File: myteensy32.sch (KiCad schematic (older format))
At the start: 31 parts, among them J1 Conn_01x14_Male, J2 Conn_01x14_Male, J3 USB_C_Receptacle_USB2.0, SW1 RESET, SW2 PROG, U1 MKL04Z32VLC4, U2 MK20DX256VLH7, U3 MCP2562-E-SN, U4 LT1117-3.3, Y2 16MHz

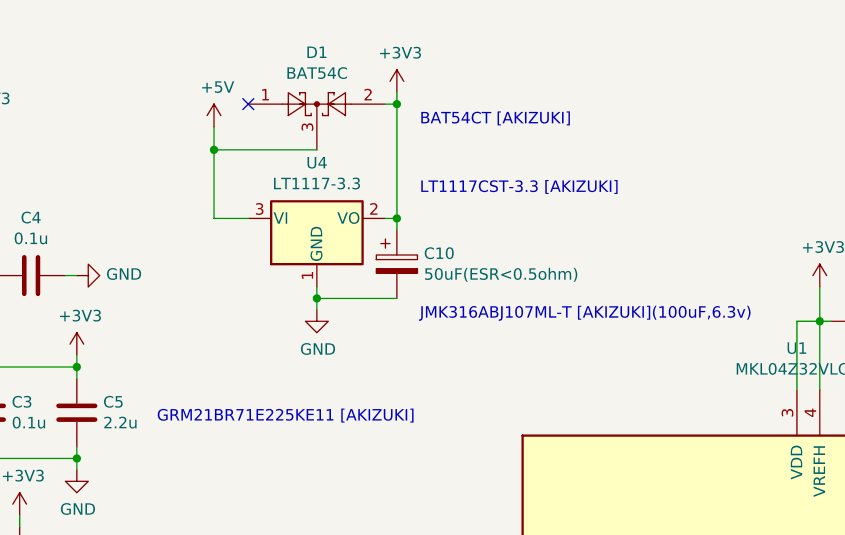
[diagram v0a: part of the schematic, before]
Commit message: 回路図中のレギュレータを変更
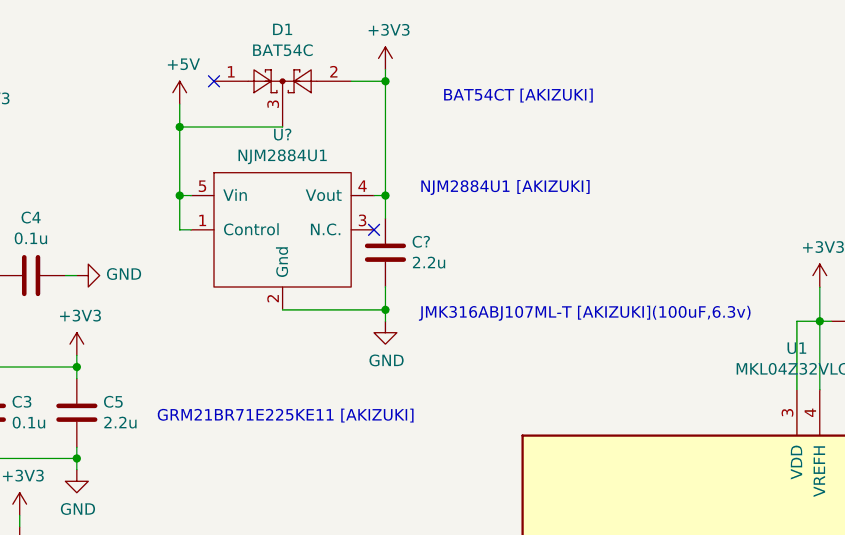
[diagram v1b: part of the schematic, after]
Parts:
- removed C10: 50uF(ESR<0.5ohm), Capacitor_SMD:C_1206_3216Metric, symbol Device:CP
- removed U4: LT1117-3.3, Package_TO_SOT_SMD:SOT-223-3_TabPin2, symbol Regulator_Linear:LT1117-3.3
- added C?: 2.2u, Capacitor_SMD:C_0805_2012Metric, symbol Device:C
- added U?: NJM2884U1, Package_TO_SOT_SMD:SOT-89-5, symbol mylib:NJM2884U1
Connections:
- net +3V3: now also C?.1, U?.4 (Vout)
- net +5V: now also U?.1 (Control), U?.5 (Vin)
- net GND: now also C?.2, U?.2 (Gnd)
- no-connect marks 30 -> 31
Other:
- note added: "NJM2884U1 [AKIZUKI]"
- note removed: "LT1117CST-3.3 [AKIZUKI]"
- moved on the sheet: D1
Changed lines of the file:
@@
 ProgramModeBtn
-$Comp
-L Regulator_Linear:LT1117-3.3 U4
-U 1 1 5F744D1C
-P 6100 1450
-F 0 "U4" H 6100 1692 50  0000 C CNN
-F 1 "LT1117-3.3" H 6100 1601 50  0000 C CNN
-F 2 "Package_TO_SOT_SMD:SOT-223-3_TabPin2" H 6100 1450 50  0001 C CNN
-F 3 "https://www.analog.com/media/en/technical-documentation/data-sheets/1117fd.pdf" H 6100 1450 50  0001 C CNN
-	1    6100 1450
-	1    0    0    -1
-$EndComp
-$Comp
-L Device:CP C10
-U 1 1 5F749F5F
-P 6450 1650
-F 0 "C10" H 6568 1696 50  0000 L CNN
-F 1 "50uF(ESR<0.5ohm)" H 6568 1605 50  0000 L CNN
-F 2 "Capacitor_SMD:C_1206_3216Metric" H 6488 1500 50  0001 C CNN
-F 3 "~" H 6450 1650 50  0001 C CNN
-	1    6450 1650
-	1    0    0    -1
-$EndComp
-Wire Wire Line
-	6450 1450 6400 1450
-Wire Wire Line
-	5800 1450 5650 1450
-Wire Wire Line
-	6450 1500 6450 1450
-Connection ~ 6450 1450
-Wire Wire Line
-	6450 1800 6100 1800
-Wire Wire Line
-	6100 1800 6100 1750
 $Comp
 L power:+3V3 #PWR0118
 U 1 1 5F7BEC67
-P 6450 900
-F 0 "#PWR0118" H 6450 750 50  0001 C CNN
-F 1 "+3V3" H 6465 1073 50  0000 C CNN
-F 2 "" H 6450 900 50  0001 C CNN
-F 3 "" H 6450 900 50  0001 C CNN
-	1    6450 900
+P 6400 800
+F 0 "#PWR0118" H 6400 650 50  0001 C CNN
+F 1 "+3V3" H 6415 973 50  0000 C CNN
+F 2 "" H 6400 800 50  0001 C CNN
+F 3 "" H 6400 800 50  0001 C CNN
+	1    6400 800
 	1    0    0    -1
 $EndComp
@@
 L power:GND #PWR0119
 U 1 1 5F7C2F97
-P 6100 1850
-F 0 "#PWR0119" H 6100 1600 50  0001 C CNN
-F 1 "GND" H 6105 1677 50  0000 C CNN
-F 2 "" H 6100 1850 50  0001 C CNN
-F 3 "" H 6100 1850 50  0001 C CNN
-	1    6100 1850
-	1    0    0    -1
-$EndComp
-Wire Wire Line
-	6100 1850 6100 1800
-Connection ~ 6100 1800
+P 6400 1900
+F 0 "#PWR0119" H 6400 1650 50  0001 C CNN
+F 1 "GND" H 6405 1727 50  0000 C CNN
+F 2 "" H 6400 1900 50  0001 C CNN
+F 3 "" H 6400 1900 50  0001 C CNN
+	1    6400 1900
+	1    0    0    -1
+$EndComp
+Wire Wire Line
+	6400 1900 6400 1850
 $Comp
 L power:+5V #PWR0120
 U 1 1 5F7C741A
-P 5650 1050
-F 0 "#PWR0120" H 5650 900 50  0001 C CNN
-F 1 "+5V" H 5665 1223 50  0000 C CNN
-F 2 "" H 5650 1050 50  0001 C CNN
-F 3 "" H 5650 1050 50  0001 C CNN
-	1    5650 1050
+P 5500 950
+F 0 "#PWR0120" H 5500 800 50  0001 C CNN
+F 1 "+5V" H 5515 1123 50  0000 C CNN
+F 2 "" H 5500 950 50  0001 C CNN
+F 3 "" H 5500 950 50  0001 C CNN
+	1    5500 950
 	1    0    0    -1
 $EndComp
@@
 MF-FSMF035X-2 [AKIZUKI]
 Text Notes 6550 1350 0    50   ~ 0
-LT1117CST-3.3 [AKIZUKI]
-Text Notes 6550 1050 0    50   ~ 0
+NJM2884U1 [AKIZUKI]
+Text Notes 6650 950  0    50   ~ 0
 BAT54CT [AKIZUKI]
 $Comp
@@
 L Diode:BAT54C D1
 U 1 1 5FA3A467
-P 6100 950
-F 0 "D1" H 6100 1175 50  0000 C CNN
-F 1 "BAT54C" H 6100 1084 50  0000 C CNN
-F 2 "Package_TO_SOT_SMD:SOT-23" H 6175 1075 50  0001 L CNN
-F 3 "http://www.diodes.com/_files/datasheets/ds11005.pdf" H 6020 950 50  0001 C CNN
-	1    6100 950
-	1    0    0    -1
-$EndComp
-Wire Wire Line
-	6450 900  6450 950
-Wire Wire Line
-	5650 1050 5650 1150
-Wire Wire Line
-	6450 950  6400 950
-Connection ~ 6450 950
-Wire Wire Line
-	6450 950  6450 1450
-Wire Wire Line
-	6100 1150 5650 1150
-Connection ~ 5650 1150
-Wire Wire Line
-	5650 1150 5650 1450
-NoConn ~ 5800 950
+P 5950 850
+F 0 "D1" H 5950 1075 50  0000 C CNN
+F 1 "BAT54C" H 5950 984 50  0000 C CNN
+F 2 "Package_TO_SOT_SMD:SOT-23" H 6025 975 50  0001 L CNN
+F 3 "http://www.diodes.com/_files/datasheets/ds11005.pdf" H 5870 850 50  0001 C CNN
+	1    5950 850
+	1    0    0    -1
+$EndComp
+Wire Wire Line
+	6400 800  6400 850
+Wire Wire Line
+	6400 850  6250 850
+Connection ~ 6400 850
+Wire Wire Line
+	6400 850  6400 1350
+NoConn ~ 5650 850
 Text Notes 10200 4400 0    50   ~ 0
 SW1020CT-ND [digikey](b3u-1000p)
@@
 NoConn ~ 4600 4000
 NoConn ~ 6100 3800
+$Comp
+L mylib:NJM2884U1 U?
+U 1 1 5FE4BD26
+P 5950 1200
+F 0 "U?" H 5950 1315 50  0000 C CNN
+F 1 "NJM2884U1" H 5950 1224 50  0000 C CNN
+F 2 "Package_TO_SOT_SMD:SOT-89-5" H 5950 1200 50  0001 C CNN
+F 3 "" H 5950 1200 50  0001 C CNN
+	1    5950 1200
+	1    0    0    -1
+$EndComp
+$Comp
+L Device:C C?
+U 1 1 5FE4CC32
+P 6400 1600
+F 0 "C?" H 6515 1646 50  0000 L CNN
+F 1 "2.2u" H 6515 1555 50  0000 L CNN
+F 2 "Capacitor_SMD:C_0805_2012Metric" H 6438 1450 50  0001 C CNN
+F 3 "~" H 6400 1600 50  0001 C CNN
+	1    6400 1600
+	1    0    0    -1
+$EndComp
+NoConn ~ 6350 1500
+Wire Wire Line
+	6350 1350 6400 1350
+Wire Wire Line
+	6400 1350 6400 1450
+Wire Wire Line
+	6400 1750 6400 1850
+Wire Wire Line
+	6400 1850 5950 1850
+Wire Wire Line
+	5550 1500 5500 1500
+Wire Wire Line
+	5500 1500 5500 1350
+Wire Wire Line
+	5500 1350 5550 1350
+Connection ~ 6400 1350
+Wire Wire Line
+	5500 950  5500 1050
+Connection ~ 5500 1350
+Wire Wire Line
+	5500 1050 5950 1050
+Connection ~ 5500 1050
+Wire Wire Line
+	5500 1050 5500 1350
+Connection ~ 6400 1850
 Wire Bus Line
 	5800 5400 5800 6800

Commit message: 固まったのでバックアップ
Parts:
- gave numbers to parts that had none: 2
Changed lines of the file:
@@
 NoConn ~ 6100 3800
 $Comp
-L mylib:NJM2884U1 U?
+L mylib:NJM2884U1 U4
 U 1 1 5FE4BD26
 P 5950 1200
-F 0 "U?" H 5950 1315 50  0000 C CNN
+F 0 "U4" H 5950 1315 50  0000 C CNN
 F 1 "NJM2884U1" H 5950 1224 50  0000 C CNN
 F 2 "Package_TO_SOT_SMD:SOT-89-5" H 5950 1200 50  0001 C CNN
@@
 $EndComp
 $Comp
-L Device:C C?
+L Device:C C10
 U 1 1 5FE4CC32
 P 6400 1600
-F 0 "C?" H 6515 1646 50  0000 L CNN
+F 0 "C10" H 6515 1646 50  0000 L CNN
 F 1 "2.2u" H 6515 1555 50  0000 L CNN
 F 2 "Capacitor_SMD:C_0805_2012Metric" H 6438 1450 50  0001 C CNN
